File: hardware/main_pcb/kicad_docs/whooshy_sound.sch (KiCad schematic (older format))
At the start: 9 parts, among them J1 audio_in, J2 audio_out, J3 extern_cutoff_CV_TRS, J4 extern_rez_CV_TRS, J5 9VDC_in, J6 signal_in, J7 signal_out, J8 cutoff_CV_in, J9 rez_CV_and_PS

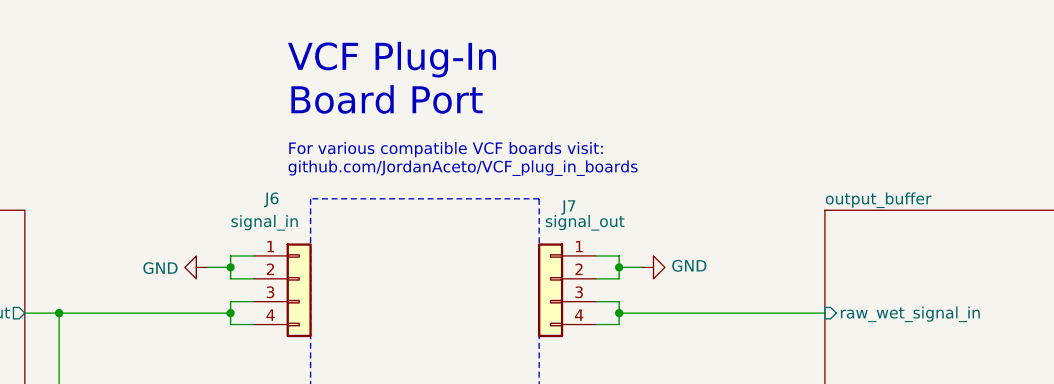
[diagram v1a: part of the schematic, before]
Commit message: center envelope follower around +1v, tidy up
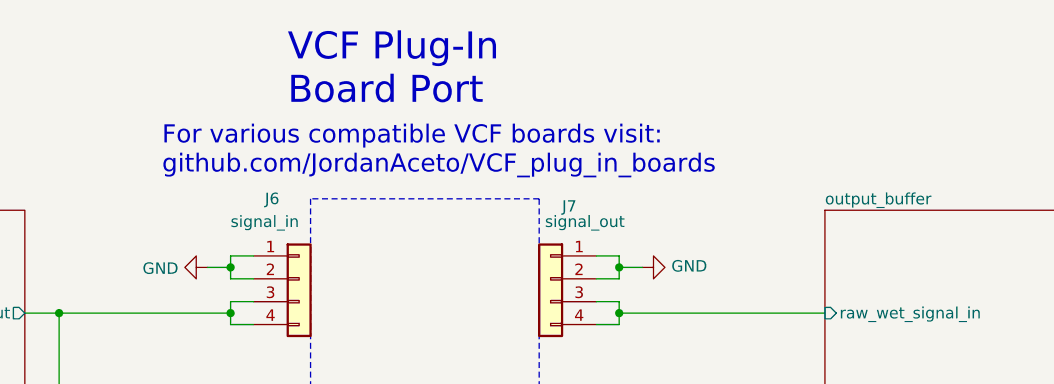
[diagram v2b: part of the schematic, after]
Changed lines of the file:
@@
 Sheet 1 8
 Title "Whooshy Sound Filter Pedal"
-Date "2021-06-29"
-Rev "0"
+Date "2021-08-05"
+Rev "0.1"
 Comp ""
 Comment1 "creativecommons.org/licenses/by/4.0/"
@@
 	-1   0    0    -1
 $EndComp
-Text Notes 5300 1500 0    118  ~ 0
+Text Notes 5300 1450 0    118  ~ 0
 VCF Plug-In \nBoard Port
-Text Notes 5300 1750 0    50   ~ 0
+Text Notes 4750 1750 0    79   ~ 0
 For various compatible VCF boards visit:\ngithub.com/JordanAceto/VCF_plug_in_boards
 Wire Wire Line
